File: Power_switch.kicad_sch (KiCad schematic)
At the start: 38 parts, among them IC409 TLP185xSE, Q409 AO3400A, Q410 HSBA8119, Q415 MMBT5551, Q416 AO3400A, Q417 HSBA8119, U400 INA219AIDCNR, U407 INA219AIDCNR, U408 INA219AIDCNR

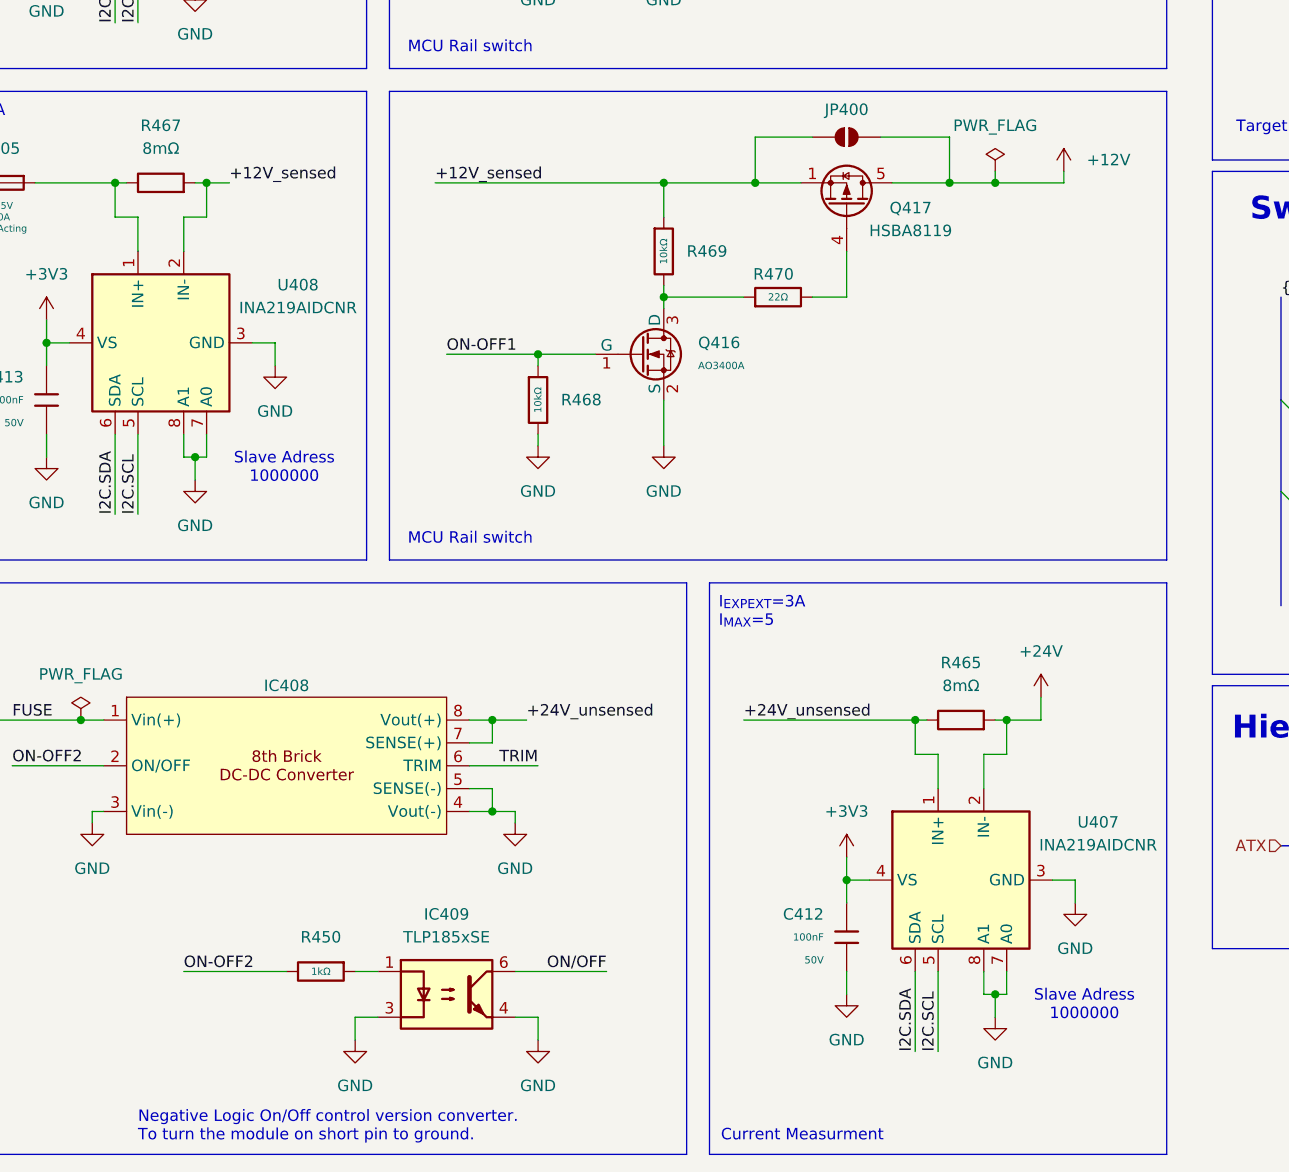
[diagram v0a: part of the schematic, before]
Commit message: added 4 pin ATX connectors
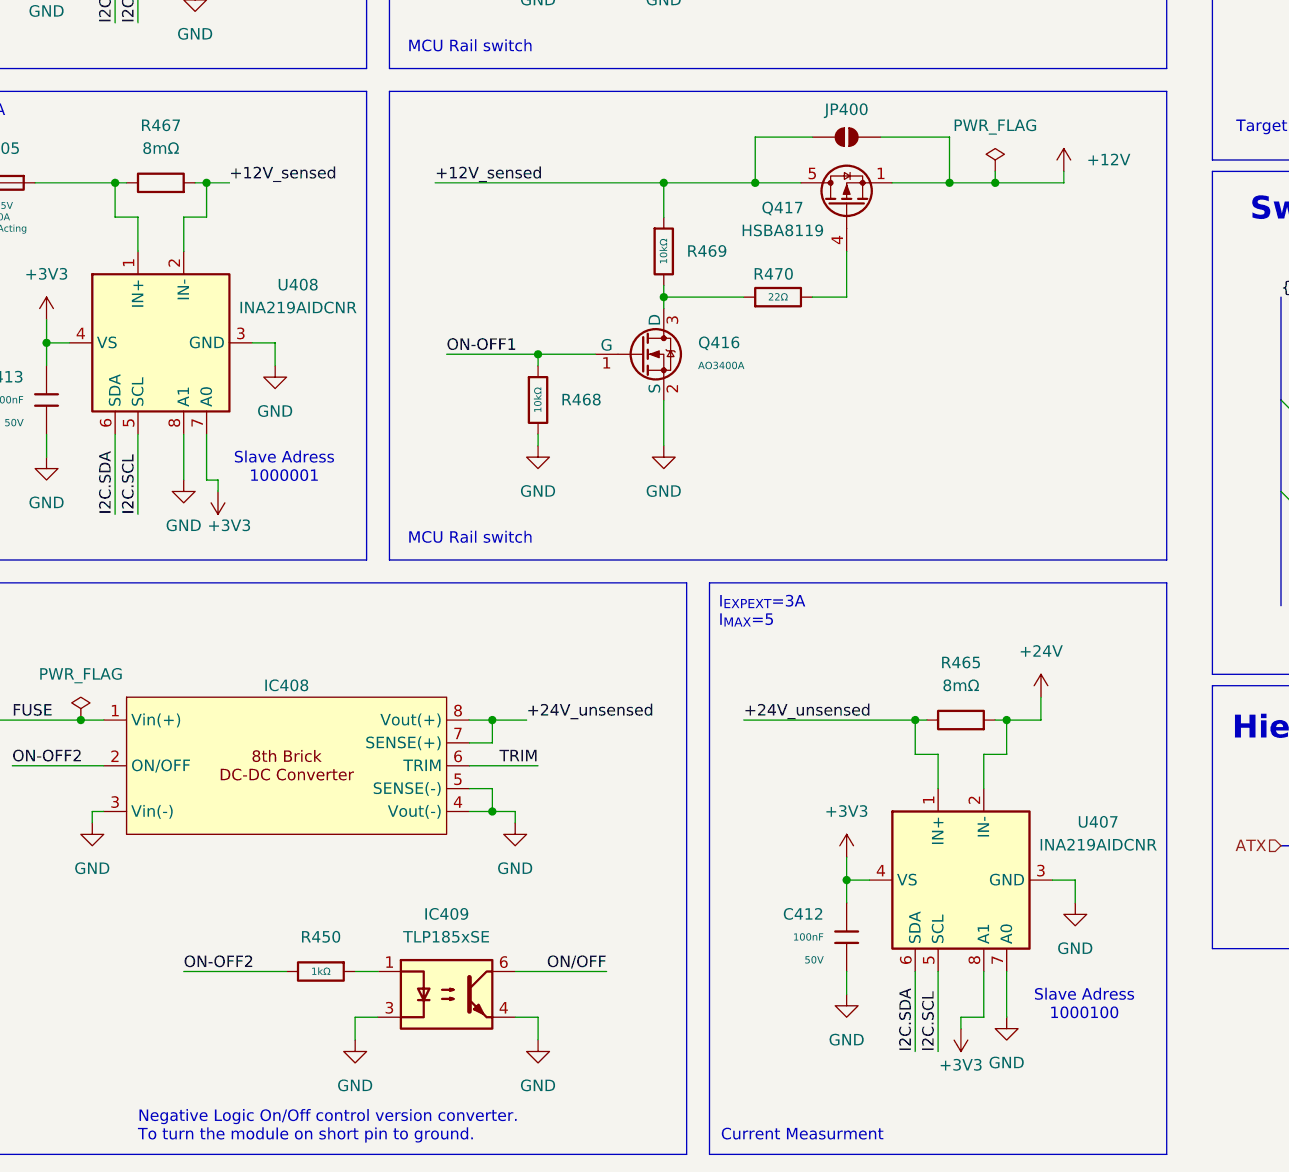
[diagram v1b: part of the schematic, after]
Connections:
- net +12V: now also Q417.1, Q417.2, Q417.3; no longer Q417.5, Q417.6, Q417.7, Q417.8, Q417.9
- net +12V_sensed: now also Q417.5, Q417.6, Q417.7, Q417.8, Q417.9; no longer Q417.1, Q417.2, Q417.3
- net +3V3: now also U407.8 (A1), U408.7 (A0)
- net GND: no longer U407.8 (A1), U408.7 (A0)
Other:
- note added: "Slave Adress 1000001"
- note added: "Slave Adress 1000100"

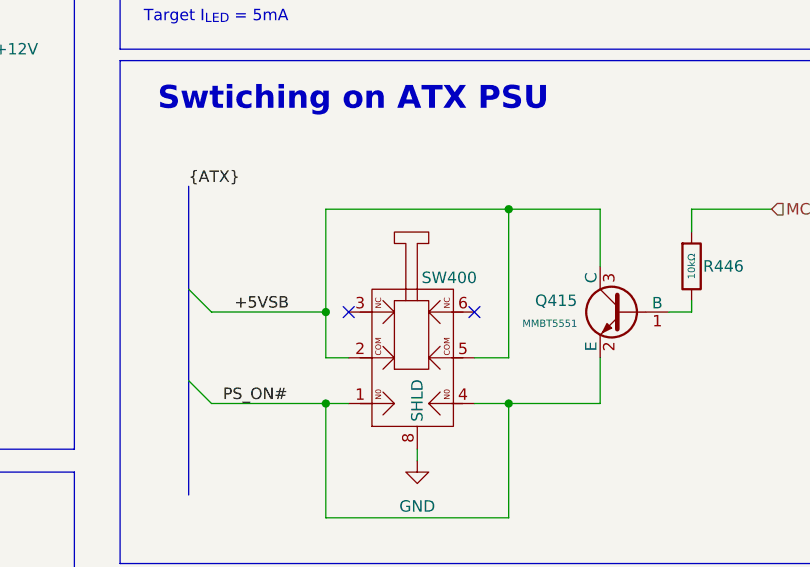
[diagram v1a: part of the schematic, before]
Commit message: fixed PS_ON# switching
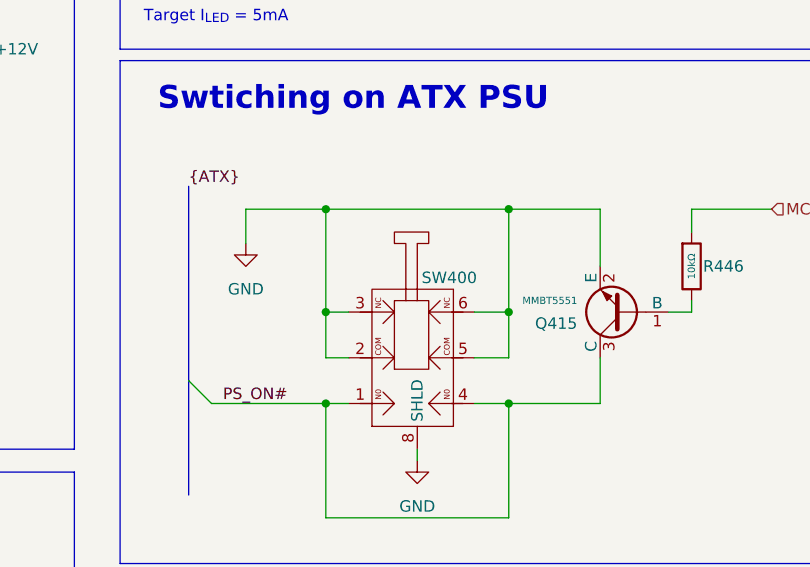
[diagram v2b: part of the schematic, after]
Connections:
- net GND: now also Q415.2 (E), SW400.2 (COM), SW400.3 (NC), SW400.5 (COM), SW400.6 (NC)
- net PS_ON#: now also Q415.3 (C); no longer Q415.2 (E)
- removed net +5VSB: Q415.3 (C), SW400.2 (COM), SW400.5 (COM)
- no-connect marks 2 -> 0
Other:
- moved on the sheet: Q415

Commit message: removed III out of IV 4 pin connector
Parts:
- JP400, JP401: footprint (none) -> Jumper:SolderJumper-2_P1.3mm_Open_RoundedPad1.0x1.5mm

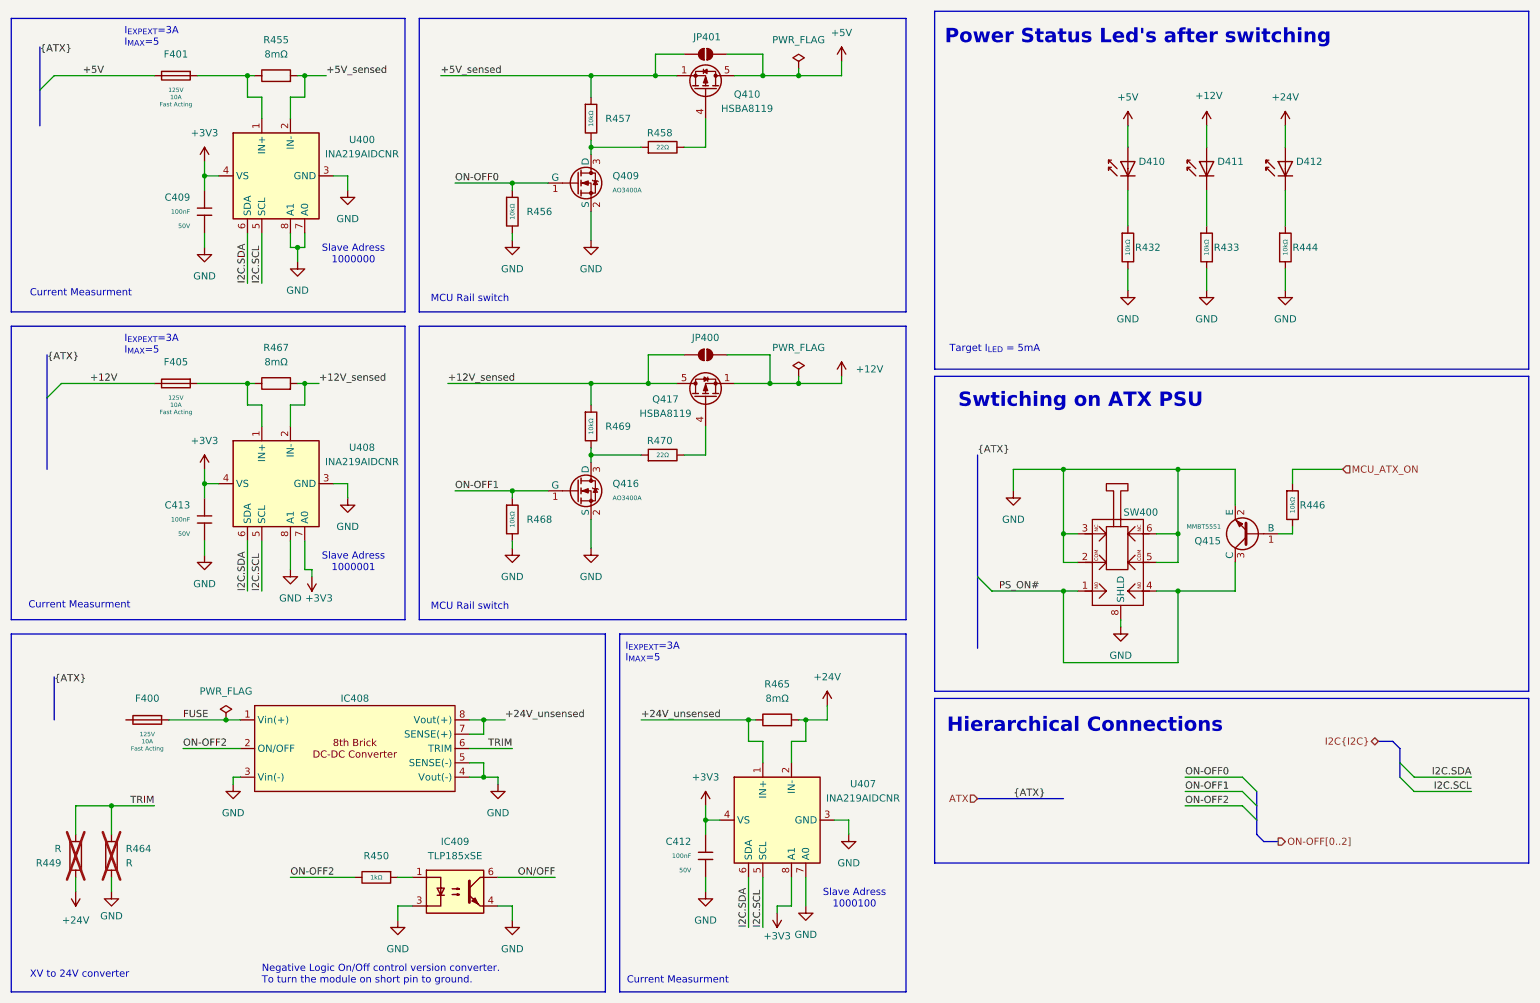
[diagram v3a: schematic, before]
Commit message: removed 3V3 converter
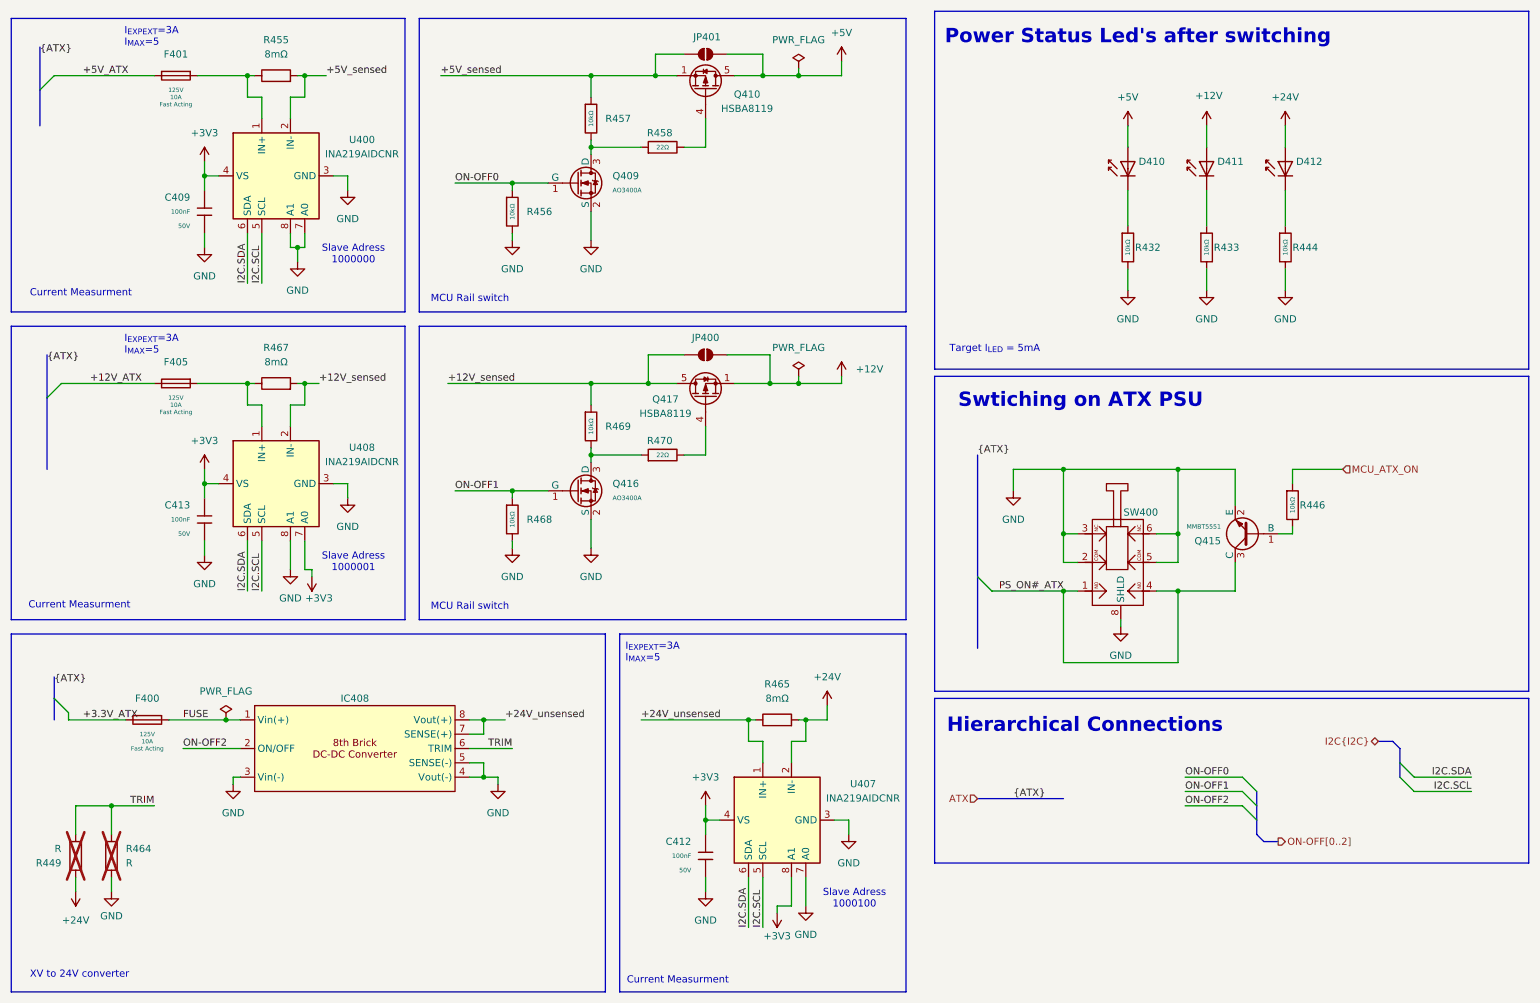
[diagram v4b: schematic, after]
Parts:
- removed IC409: TLP185xSE, Package_SO:SOIC-4_4.55x3.7mm_P2.54mm, symbol Isolator:TLP185xSE
- removed R450: 1kΩ, PCM_JLCPCB:R_0402, symbol PCM_JLCPCB-Resistors:0402,1kΩ
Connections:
- net +12V: no longer F405.2
- net +5V: no longer F401.2
- net +3.3V_ATX: now reaches F400.2
- net PS_ON# renamed PS_ON#_ATX
- new net +12V_ATX: F405.2
- new net +5V_ATX: F401.2
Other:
- note removed: "Negative Logic On/Off control version converter. To turn the module on short pin to ground."

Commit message: routing progress
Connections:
- net +12V: now also Q417.5, Q417.6, Q417.7, Q417.8, Q417.9; no longer Q417.1, Q417.2, Q417.3
- net +12V_sensed: now also Q417.1, Q417.2, Q417.3; no longer Q417.5, Q417.6, Q417.7, Q417.8, Q417.9
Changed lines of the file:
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@@
 	)
 	(junction
-		(at 153.67 78.74)
-		(diameter 0)
-		(color 0 0 0 0)
-	)
-	(junction
 		(at 220.98 93.98)
 		(diameter 0)
@@
 	)
 	(junction
-		(at 153.67 24.13)
-		(diameter 0)
-		(color 0 0 0 0)
-	)
-	(junction
 		(at 116.84 78.74)
 		(diameter 0)
@@
 	(wire
 		(pts
-			(xy 153.67 22.86) (xy 153.67 24.13)
-		)
-		(stroke
-			(width 0)
-			(type default)
-		)
-	)
-	(wire
-		(pts
 			(xy 53.34 148.59) (xy 54.61 148.59)
 		)
@@
 	(wire
 		(pts
-			(xy 147.32 24.13) (xy 153.67 24.13)
-		)
-		(stroke
-			(width 0)
-			(type default)
-		)
-	)
-	(wire
-		(pts
 			(xy 220.98 93.98) (xy 220.98 105.41)
 		)
@@
 	(wire
 		(pts
-			(xy 153.67 77.47) (xy 153.67 78.74)
-		)
-		(stroke
-			(width 0)
-			(type default)
-		)
-	)
-	(wire
-		(pts
-			(xy 153.67 78.74) (xy 161.29 78.74)
+			(xy 148.59 78.74) (xy 161.29 78.74)
 		)
 		(stroke
@@
 		)
 	)
-	(wire
-		(pts
-			(xy 148.59 78.74) (xy 153.67 78.74)
-		)
-		(stroke
-			(width 0)
-			(type default)
-		)
-	)
 	(bus
 		(pts
-			(xy 185.42 152.4) (xy 200.66 152.4)
+			(xy 189.23 152.4) (xy 204.47 152.4)
 		)
 		(stroke
@@
 	(wire
 		(pts
-			(xy 153.67 24.13) (xy 161.29 24.13)
+			(xy 147.32 24.13) (xy 161.29 24.13)
 		)
 		(stroke
@@
 	)
 	(label "{ATX}"
-		(at 191.77 152.4 0)
+		(at 195.58 152.4 0)
 		(effects
 			(font
@@
 		)
 	)
-	(hierarchical_label "ATX"
+	(hierarchical_label "ATX{ATX}"
 		(shape input)
-		(at 185.42 152.4 180)
+		(at 189.23 152.4 180)
 		(effects
 			(font
@@
 	)
 	(symbol
-		(lib_id "power:PWR_FLAG")
-		(at 153.67 77.47 0)
-		(unit 1)
-		(exclude_from_sim no)
-		(in_bom yes)
-		(on_board yes)
-		(dnp no)
-		(fields_autoplaced yes)
-		(property "Reference" "#FLG0407"
-			(at 153.67 75.565 0)
-			(effects
-				(font
-					(size 1.27 1.27)
-				)
-				(hide yes)
-			)
-		)
-		(property "Value" "PWR_FLAG"
-			(at 153.67 72.39 0)
-			(effects
-				(font
-					(size 1.27 1.27)
-				)
-			)
-		)
-		(property "Footprint" ""
-			(at 153.67 77.47 0)
-			(effects
-				(font
-					(size 1.27 1.27)
-				)
-				(hide yes)
-			)
-		)
-		(property "Datasheet" "~"
-			(at 153.67 77.47 0)
-			(effects
-				(font
-					(size 1.27 1.27)
-				)
-				(hide yes)
-			)
-		)
-		(property "Description" "Special symbol for telling ERC where power comes from"
-			(at 153.67 77.47 0)
-			(effects
-				(font
-					(size 1.27 1.27)
-				)
-				(hide yes)
-			)
-		)
-		(pin "1"
-		)
-		(instances
-			(project "ATX_PSU"
-				(path "/090a8e41-87a8-4fb1-998b-60a2c0dc4cee/eabd1460-37fc-4011-96d2-589aebf98c67"
-					(reference "#FLG0407")
-					(unit 1)
-				)
-			)
-		)
-	)
-	(symbol
 		(lib_id "power:GND")
 		(at 137.16 168.91 0)
@@
 		(lib_id "MCAC80P06YHE3:MCAC80P06YHE3")
 		(at 137.16 78.74 0)
+		(mirror y)
 		(unit 1)
 		(exclude_from_sim no)
@@
 		(dnp no)
 		(property "Reference" "Q417"
-			(at 130.048 81.534 0)
+			(at 144.272 81.534 0)
 			(effects
 				(font
@@
 		)
 		(property "Value" "HSBA8119"
-			(at 130.048 84.074 0)
+			(at 144.272 84.074 0)
 			(effects
 				(font
@@
 		)
 		(property "Footprint" "DFN5060-8L:DFN5060-8L"
-			(at 144.78 85.852 0)
+			(at 129.54 85.852 0)
 			(effects
 				(font
@@
 		)
 		(property "Datasheet" "https://www.lcsc.com/product-detail/C22359243.html"
-			(at 144.78 85.852 0)
+			(at 129.54 85.852 0)
 			(effects
 				(font
@@
 		)
 		(property "Description" "80V 70A 145W 15mΩ@10V 2.5V@250uA 1 P-Channel PRPAK5x6-8L MOSFETs ROHS"
-			(at 144.78 85.852 0)
+			(at 129.54 85.852 0)
 			(effects
 				(font
@@
 					(unit 1)
 				)
-			)
-		)
-	)
-	(symbol
-		(lib_id "power:PWR_FLAG")
-		(at 153.67 22.86 0)
-		(unit 1)
-		(exclude_from_sim no)
-		(in_bom yes)
-		(on_board yes)
-		(dnp no)
-		(fields_autoplaced yes)
-		(property "Reference" "#FLG0400"
-			(at 153.67 20.955 0)
-			(effects
-				(font
-					(size 1.27 1.27)
-				)
-				(hide yes)
-			)
-		)
-		(property "Value" "PWR_FLAG"
-			(at 153.67 17.78 0)
-			(effects
-				(font
-					(size 1.27 1.27)
-				)
-			)
-		)
-		(property "Footprint" ""
-			(at 153.67 22.86 0)
-			(effects
-				(font
-					(size 1.27 1.27)
-				)
-				(hide yes)
-			)
-		)
-		(property "Datasheet" "~"
-			(at 153.67 22.86 0)
-			(effects
-				(font
-					(size 1.27 1.27)
-				)
-				(hide yes)
-			)
-		)
-		(property "Description" "Special symbol for telling ERC where power comes from"
-			(at 153.67 22.86 0)
-			(effects
-				(font
-					(size 1.27 1.27)
-				)
-				(hide yes)
-			)
-		)
-		(pin "1"
-		)
-		(instances
-			(project "ATX_PSU"
-				(path "/090a8e41-87a8-4fb1-998b-60a2c0dc4cee/eabd1460-37fc-4011-96d2-589aebf98c67"
-					(reference "#FLG0400")
-					(unit 1)
-				)

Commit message: finished routing
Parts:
- removed SW400: ~, PS-22F03:SW-TH_G-SWITCH-PS-22F03N, symbol PS-22F03:PS-22F03
- added SW401: SW_SPDT, Button_Switch_SMD:SW_SPDT_CK_JS102011SAQN, symbol Switch:SW_SPDT
- IC408: now not fitted
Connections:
- net GND: now also SW401.1 (A)
- net PS_ON#_ATX: now also SW401.2 (B)
- no-connect marks 0 -> 1
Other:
- note added: "I_{MAX}=7A"
- moved on the sheet: Q415, R446

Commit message: finished PCB
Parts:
- SW401: footprint Button_Switch_SMD:SW_SPDT_CK_JS102011SAQN -> Button_Switch_THT:SW_Slide-03_Wuerth-WS-SLTV_10x2.5x6.4_P2.54mm
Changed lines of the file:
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@@
 			)
 		)
-		(property "Footprint" "Button_Switch_SMD:SW_SPDT_CK_JS102011SAQN"
+		(property "Footprint" "Button_Switch_THT:SW_Slide-03_Wuerth-WS-SLTV_10x2.5x6.4_P2.54mm"
 			(at 208.28 111.76 0)
 			(effects
